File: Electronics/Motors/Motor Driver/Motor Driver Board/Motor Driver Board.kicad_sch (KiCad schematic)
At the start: 4 parts

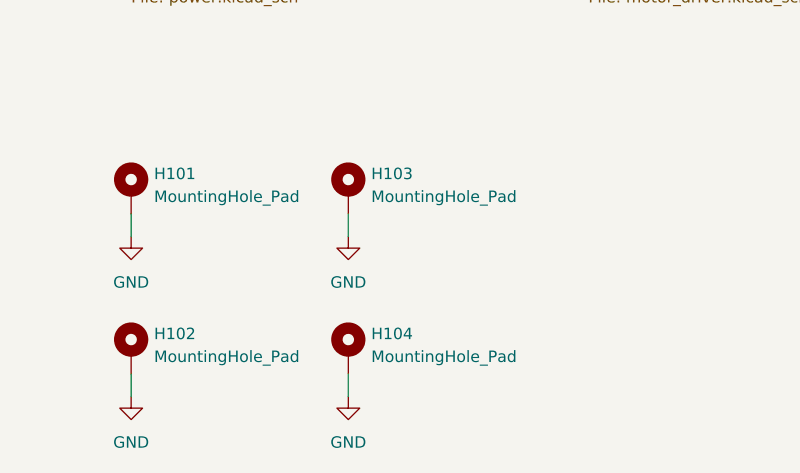
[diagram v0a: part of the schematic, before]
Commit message: PCB layout progress, spice simulations for power board
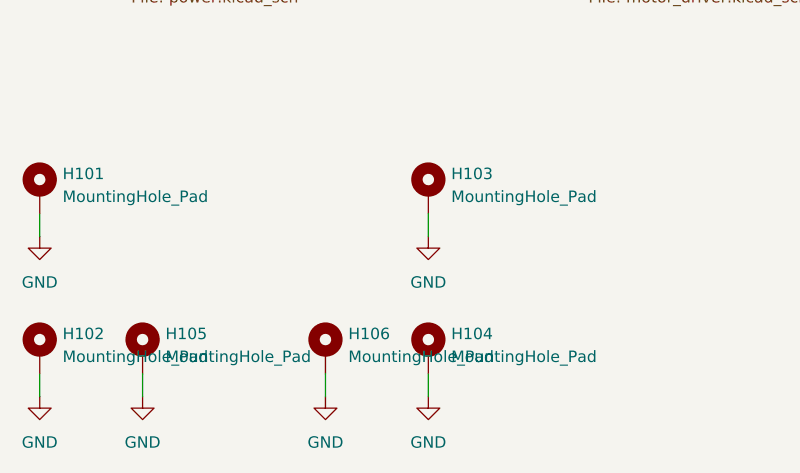
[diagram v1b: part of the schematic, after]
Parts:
- added H105, H106: MountingHole_Pad, MountingHole:MountingHole_3.2mm_M3_DIN965_Pad, symbol Mechanical:MountingHole_Pad
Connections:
- net GND: now also H105.1, H106.1
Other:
- moved on the sheet: H101, H102, H103, H104

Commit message: Sensor hub board done
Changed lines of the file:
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@@
+    (stroke (width 0) (type default))
+  )
+  (wire (pts (xy 85.09 114.3) (xy 77.47 114.3))
     (stroke (width 0) (type default))
   )
@@
     (stroke (width 0) (type default))
   )
+  (wire (pts (xy 85.09 111.76) (xy 85.09 114.3))
+    (stroke (width 0) (type default))
+  )
+  (wire (pts (xy 77.47 114.3) (xy 77.47 111.76))
+    (stroke (width 0) (type default))
+  )
   (wire (pts (xy 54.61 124.46) (xy 54.61 121.92))
     (stroke (width 0) (type default))
@@
     )
   )
+  (symbol (lib_id "power:+3V3") (at 85.09 111.76 0) (unit 1)
+    (in_bom yes) (on_board yes) (dnp no) (fields_autoplaced)
+    (property "Reference" "#PWR0108" (at 85.09 115.57 0)
+      (effects (font (size 1.27 1.27)) hide)
+    )
+    (property "Value" "+3V3" (at 85.09 107.95 0)
+      (effects (font (size 1.27 1.27)))
+    )
+    (property "Footprint" "" (at 85.09 111.76 0)
+      (effects (font (size 1.27 1.27)) hide)
+    )
+    (property "Datasheet" "" (at 85.09 111.76 0)
+      (effects (font (size 1.27 1.27)) hide)
+    )
+    (pin "1")
+    (instances
+      (project "Motor Driver Board"
+        (path "/5318664d-e328-4e84-a383-7318275dc447"
+          (reference "#PWR0108") (unit 1)
+        )
+      )
+    )
+  )
   (symbol (lib_id "Mechanical:MountingHole_Pad") (at 22.86 119.38 0) (unit 1)
     (in_bom yes) (on_board yes) (dnp no) (fields_autoplaced)
@@
         )
       )
+    )
+  )
+  (symbol (lib_id "power:+3.3V") (at 77.47 111.76 0) (unit 1)
+    (in_bom yes) (on_board yes) (dnp no) (fields_autoplaced)
+    (property "Reference" "#PWR0107" (at 77.47 115.57 0)
+      (effects (font (size 1.27 1.27)) hide)
+    )
+    (property "Value" "+3.3V" (at 77.47 107.95 0)
+      (effects (font (size 1.27 1.27)))
+    )
+    (property "Footprint" "" (at 77.47 111.76 0)
+      (effects (font (size 1.27 1.27)) hide)
+    )
+    (property "Datasheet" "" (at 77.47 111.76 0)
+      (effects (font (size 1.27 1.27)) hide)
+    )
+    (pin "1")
+    (instances
+      (project "Motor Driver Board"
+        (path "/5318664d-e328-4e84-a383-7318275dc447"
+          (reference "#PWR0107") (unit 1)
+        )
+      )

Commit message: All boards done
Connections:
- removed net GND: H101.1, H102.1, H103.1, H104.1, H105.1, H106.1
- no-connect marks 0 -> 6
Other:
- moved on the sheet: H101, H102, H103, H104, H105, H106
